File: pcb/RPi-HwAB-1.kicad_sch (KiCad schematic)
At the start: 5 parts, among them U1 CAT24C256

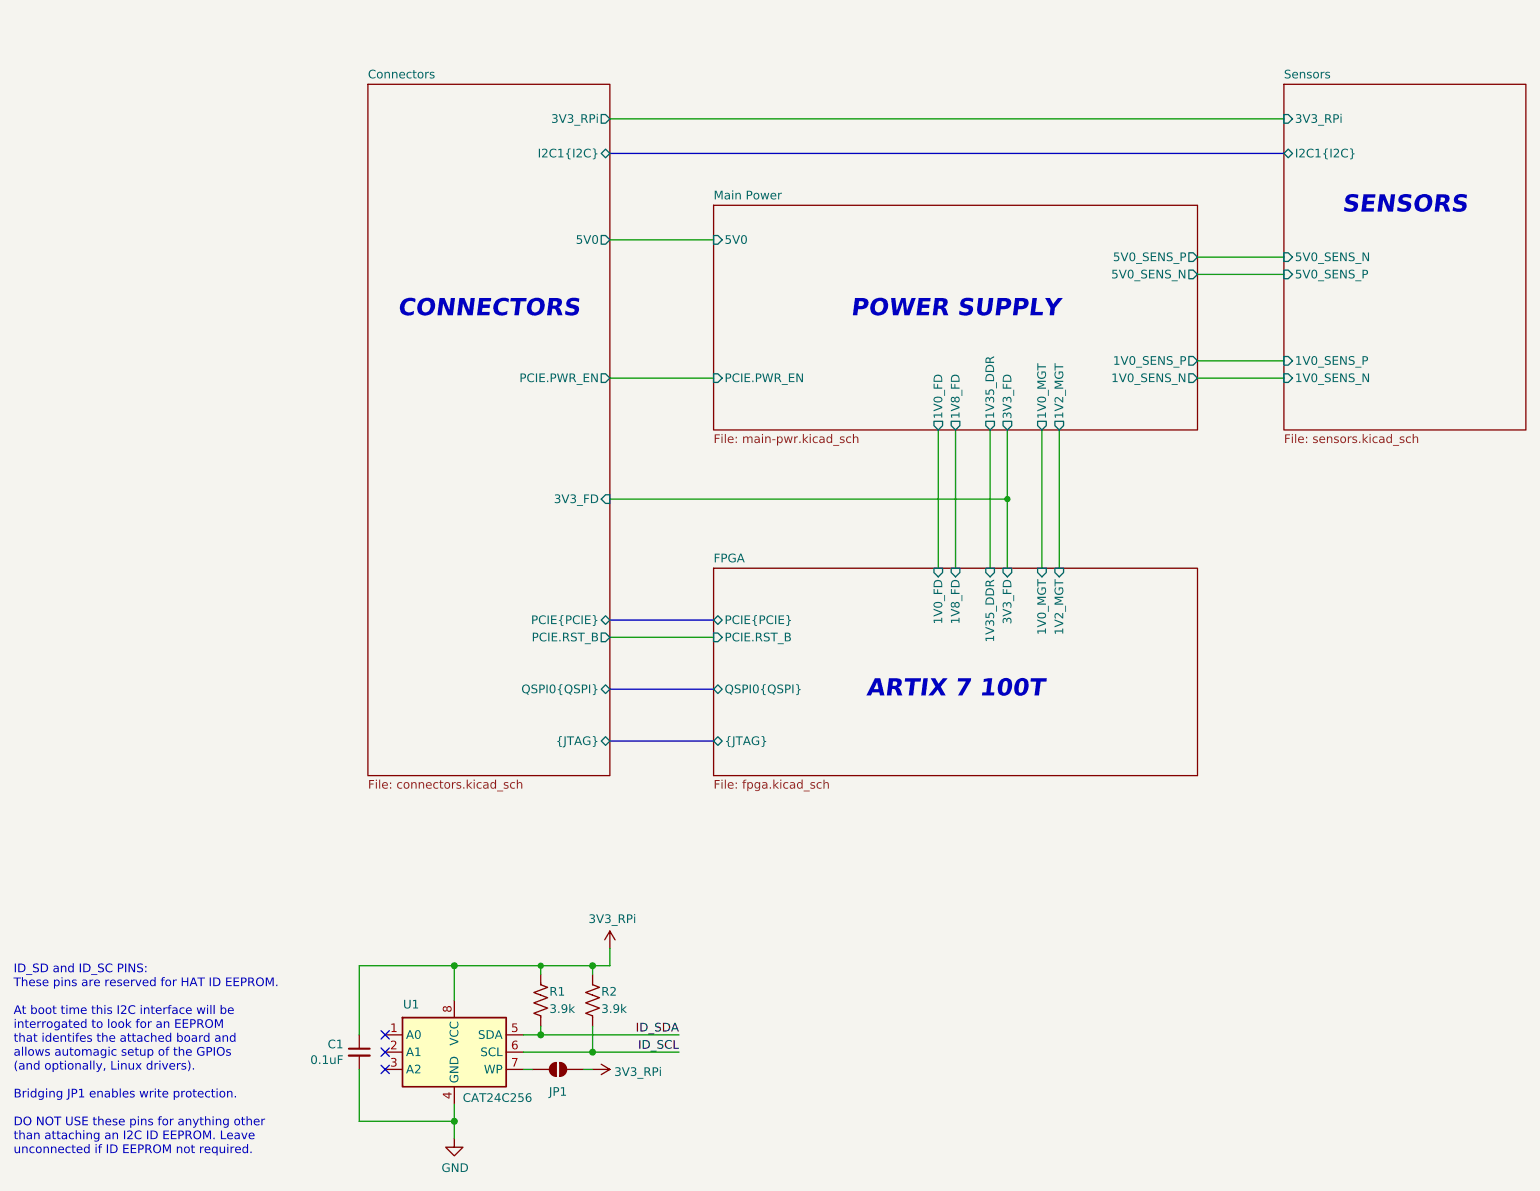
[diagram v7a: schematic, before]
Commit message: dogbone for ddr
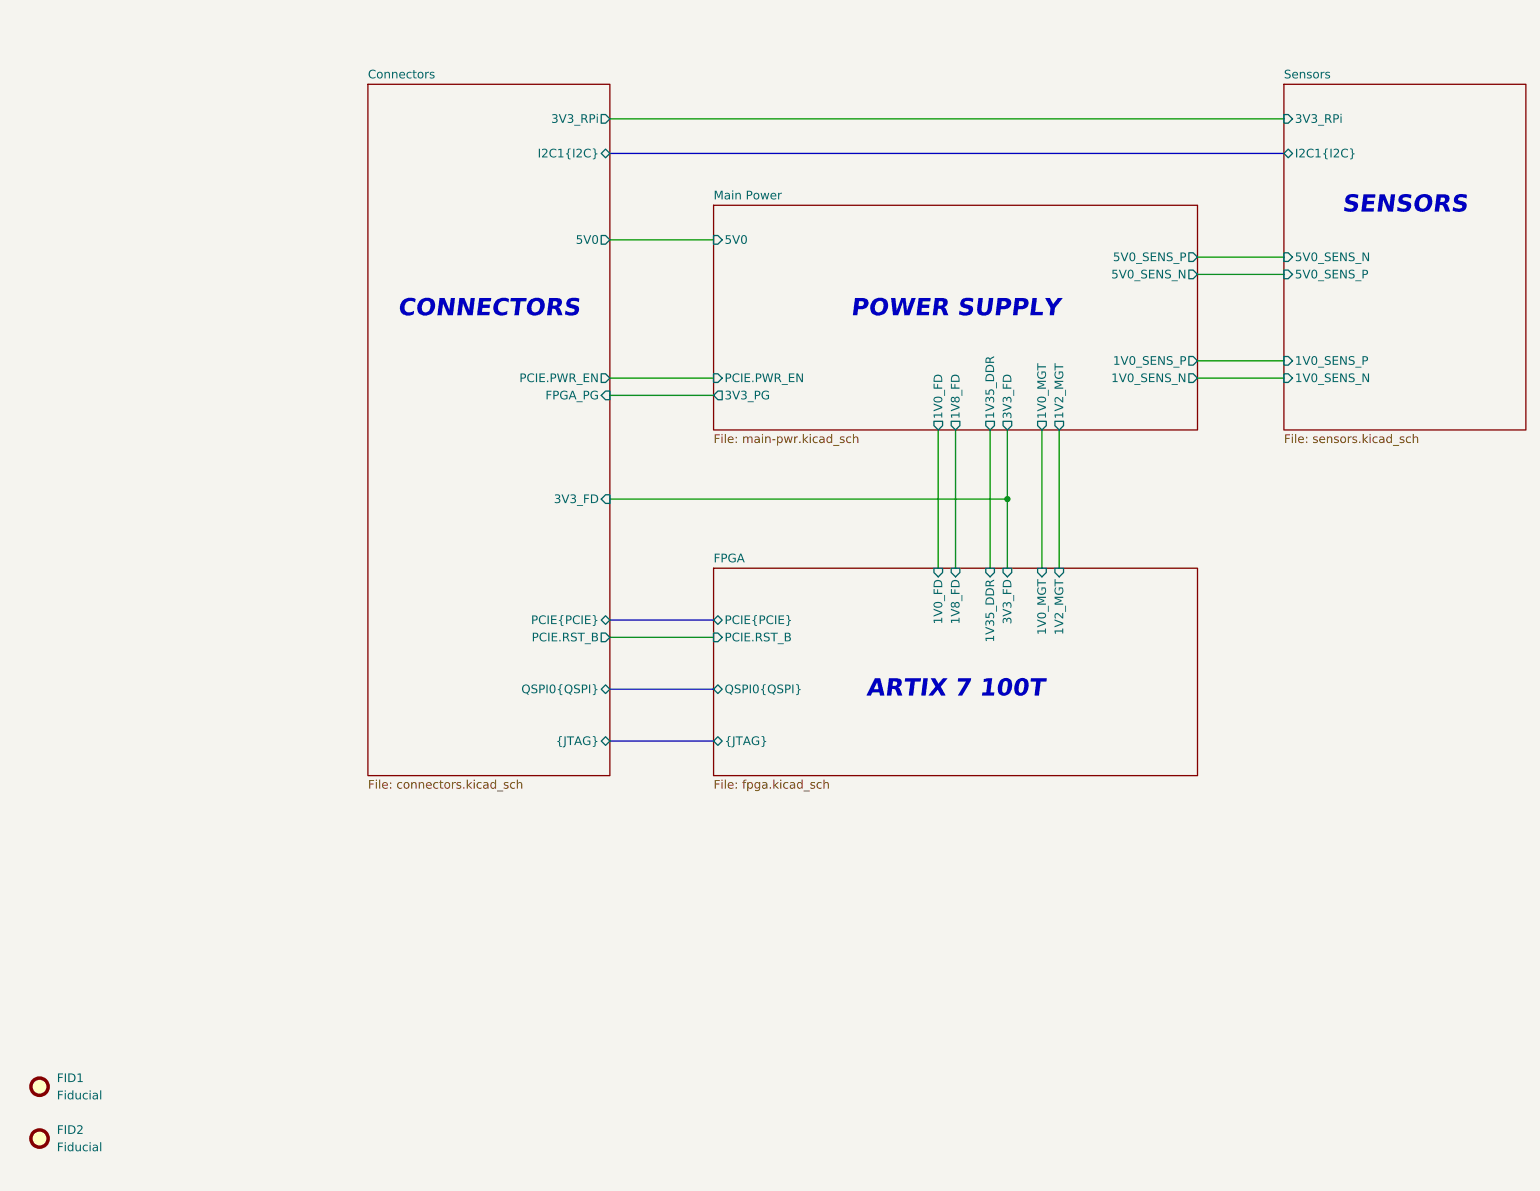
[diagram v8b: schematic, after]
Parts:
- removed C1: 0.1uF, Capacitor_SMD:C_0402_1005Metric, symbol library:C_Small
- removed JP1: ID_WP, Jumper:SolderJumper-2_P1.3mm_Open_Pad1.0x1.5mm, symbol library:SolderJumper_2_Open
- removed R1, R2: 3.9k, Resistor_SMD:R_0402_1005Metric, symbol library:R_US
- removed U1: CAT24C256, Package_DFN_QFN:DFN-8-1EP_3x2mm_P0.5mm_EP1.7x1.4mm, symbol library:CAT24C256
- added FID1, FID2: Fiducial, Fiducial:Fiducial_1.5mm_Mask4.5mm, symbol Mechanical:Fiducial
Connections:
- no-connect marks 3 -> 0
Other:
- sheet Connectors ports: added FPGA_PG; removed none
- sheet Main Power ports: added 3V3_PG; removed none
- note removed: "ID_SD and ID_SC PINS: These pins are reserved for HAT ID EEPROM. At boot time this I2C interface will be interrogated to look for an EEPROM that identifes the attached board and allows automagic setup of the GPIOs (and optionally, Linux drivers). Bridging JP1 enables write protection. DO NOT USE these pins for anything other than attaching an I2C ID EEPROM. Leave unconnected if ID EEPROM not requ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"
